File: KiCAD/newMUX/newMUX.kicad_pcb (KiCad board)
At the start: 4 copper layers, 40 x 89 mm, 36 parts, among them J1 Conn_01x14, J2 Conn_02x06_Odd_Even, J3 Conn_02x06_Odd_Even, J4 Conn_01x14, U1 ASSR-1611, U10 ASSR-1611, U11 ASSR-1611, U12 ASSR-1611, U13 ASSR-1611, U14 ASSR-1611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

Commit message: wip for base1x
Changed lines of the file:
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@@
   (general
     (thickness 1.6)
-    (drawings 9)
+    (drawings 17)
     (tracks 698)
     (zones 0)
@@
     (tags "resistor 2010")
     (attr smd)
-    (fp_text reference R1 (at 0 2.54 90) (layer F.SilkS)
+    (fp_text reference R1 (at 0.81 -2.7 90) (layer F.SilkS)
       (effects (font (size 1 1) (thickness 0.15)))
     )
@@
       (xy 8.293997 0.976563) (xy 8.491005 0.779554)) (layer F.SilkS) (width 0.001))
   )
+  (gr_line (start 14 14) (end 14 -14) (layer F.SilkS) (width 0.2))
+  (gr_line (start -14 14) (end 14 14) (layer F.SilkS) (width 0.2))
+  (gr_line (start -14 -14) (end -14 14) (layer F.SilkS) (width 0.2))
+  (gr_line (start 14 -14) (end -14 -14) (layer F.SilkS) (width 0.2))
+  (gr_line (start -15 15) (end -15 -15) (layer F.SilkS) (width 0.2))
+  (gr_line (start 15 15) (end -15 15) (layer F.SilkS) (width 0.2))
+  (gr_line (start 15 -15) (end 15 15) (layer F.SilkS) (width 0.2))
+  (gr_line (start -15 -15) (end 15 -15) (layer F.SilkS) (width 0.2))
   (gr_arc (start 17.5 42) (end 17.5 44.5) (angle -90) (layer Edge.Cuts) (width 0.15))
   (gr_arc (start -17.5 42) (end -20 42) (angle -90) (layer Edge.Cuts) (width 0.15))

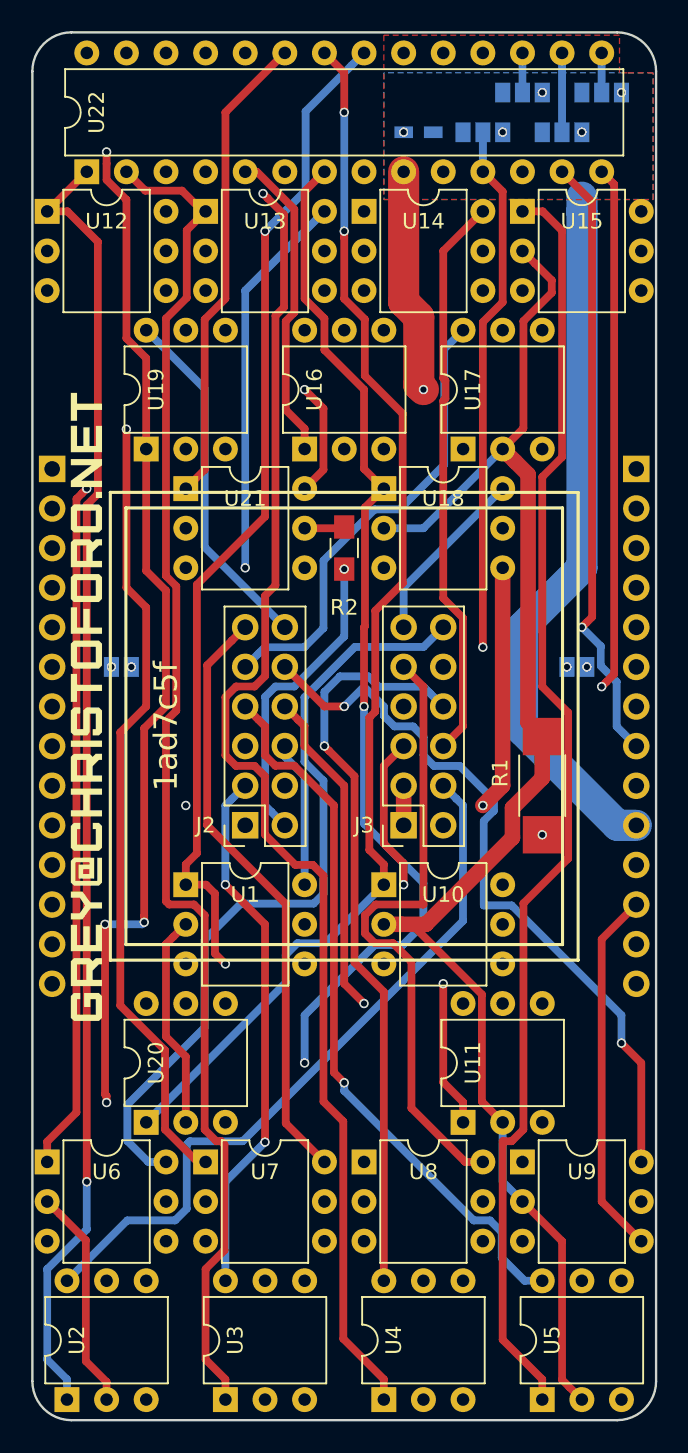
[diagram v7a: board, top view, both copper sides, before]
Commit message: make spring pin board pin holders smaller, update base1x, update mux design controller board
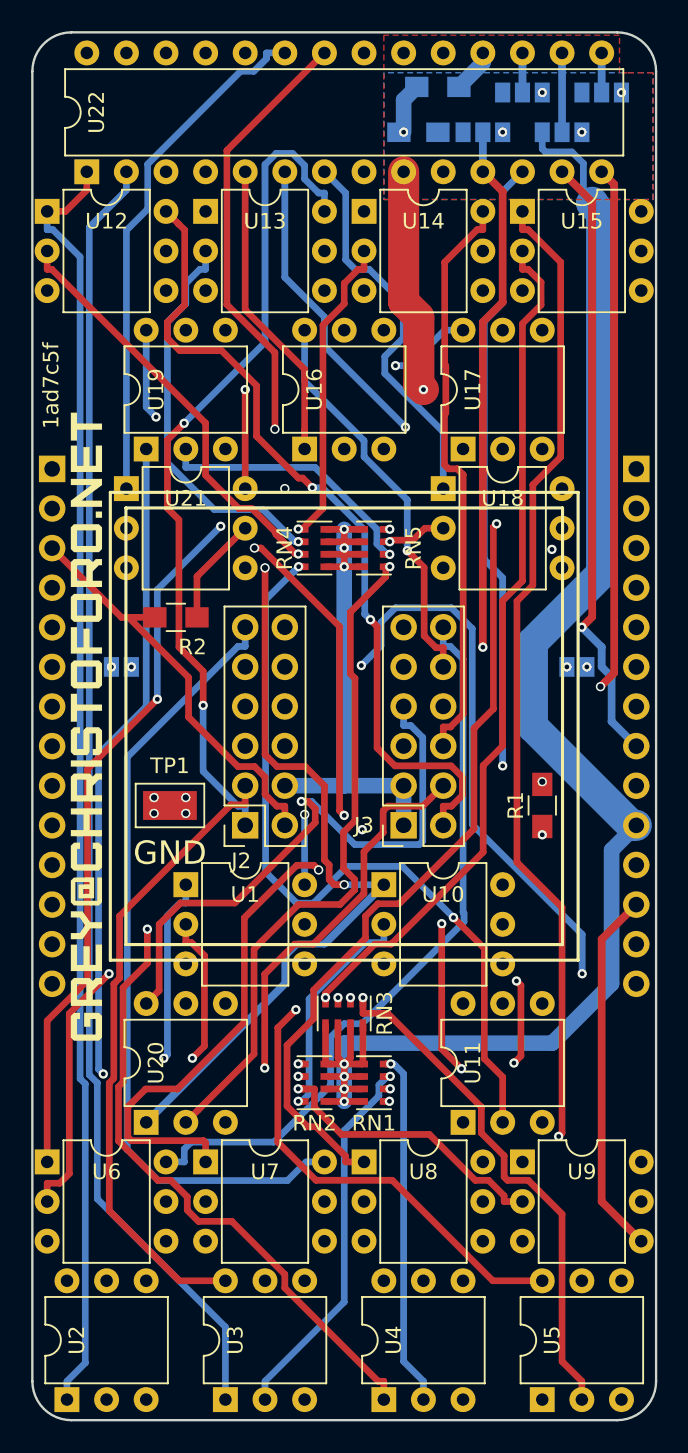
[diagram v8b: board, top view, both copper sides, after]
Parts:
- added R3: 10K, Resistors_SMD:R_0805_HandSoldering, B.Cu at (6.00, -41.0)
- added RN1: 470R, Resistors_SMD:R_Cat16-4, F.Cu at (1.91, 22.9)
- added RN2: 470R, Resistors_SMD:R_Cat16-4, F.Cu at (-1.91, 22.9)
- added RN3: 470R, Resistors_SMD:R_Cat16-4, F.Cu at (0.00, 18.4)
- added RN4: 470R, Resistors_SMD:R_Cat16-4, F.Cu at (-1.91, -11.4)
- added RN5: 470R, Resistors_SMD:R_Cat16-4, F.Cu at (1.91, -11.4)
- added TP1: Test_Point, myParts:Test_Point_S1751-46R, F.Cu at (-11.2, 5.08)
- C1: footprint Capacitors_SMD:C_0603_HandSoldering -> Capacitors_SMD:C_0805_HandSoldering
- R1: value 830K -> 470R; footprint Resistors_SMD:R_2010_HandSoldering -> Resistors_SMD:R_0805_HandSoldering
- moved R2 11.7 mm to (-10.8, -6.99), turned to 180 degrees
- moved U21 3.81 mm to (-14.0, -15.2)
- moved U18 3.81 mm to (6.35, -15.2)
- moved L1 1.27 mm to (-16.5, 0.00)
- moved R1 1.27 mm to (12.7, 5.08)
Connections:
- R1 pad 2: /PRE_GND -> Net-(R1-Pad2)
- U1 pad 2: /PRE_GND -> Net-(RN1-Pad1)
- U1 pad 3: Net-(U1-Pad3) -> (no net)
- U1 pad 5: Net-(U1-Pad5) -> (no net)
- U10 pad 2: /PRE_GND -> Net-(RN2-Pad8)
- U10 pad 3: Net-(U10-Pad3) -> (no net)
- U10 pad 5: Net-(U10-Pad5) -> (no net)
- U11 pad 2: /PRE_GND -> Net-(RN4-Pad4)
- U11 pad 3: Net-(U11-Pad3) -> (no net)
- U11 pad 5: Net-(U11-Pad5) -> (no net)
- U12 pad 2: /PRE_GND -> Net-(RN4-Pad3)
- U12 pad 3: Net-(U12-Pad3) -> (no net)
- U12 pad 5: Net-(U12-Pad5) -> (no net)
- U13 pad 2: /PRE_GND -> Net-(RN4-Pad2)
- U13 pad 3: Net-(U13-Pad3) -> (no net)
- U13 pad 5: Net-(U13-Pad5) -> (no net)
- U14 pad 2: /PRE_GND -> Net-(RN4-Pad1)
- U14 pad 3: Net-(U14-Pad3) -> (no net)
- U14 pad 5: Net-(U14-Pad5) -> (no net)
- U15 pad 2: /PRE_GND -> Net-(RN3-Pad4)
- U15 pad 3: Net-(U15-Pad3) -> (no net)
- U15 pad 5: Net-(U15-Pad5) -> (no net)
- U16 pad 2: /PRE_GND -> Net-(RN3-Pad3)
- U16 pad 3: Net-(U16-Pad3) -> (no net)
- U16 pad 5: Net-(U16-Pad5) -> (no net)
- U17 pad 2: /PRE_GND -> Net-(RN5-Pad8)
- U17 pad 3: Net-(U17-Pad3) -> (no net)
- U17 pad 5: Net-(U17-Pad5) -> (no net)
- U18 pad 2: /PRE_GND -> Net-(RN5-Pad7)
- U18 pad 3: Net-(U18-Pad3) -> (no net)
- U18 pad 5: Net-(U18-Pad5) -> (no net)
- U19 pad 2: /PRE_GND -> Net-(RN5-Pad6)
- U19 pad 3: Net-(U19-Pad3) -> (no net)
- U19 pad 5: Net-(U19-Pad5) -> (no net)
- U2 pad 2: /PRE_GND -> Net-(RN1-Pad2)
- U2 pad 3: Net-(U2-Pad3) -> (no net)
- U2 pad 5: Net-(U2-Pad5) -> (no net)
- U20 pad 2: /PRE_GND -> Net-(RN5-Pad5)
- U20 pad 3: Net-(U20-Pad3) -> (no net)
- U20 pad 5: Net-(U20-Pad5) -> (no net)
- U21 pad 2: /PRE_GND -> Net-(R1-Pad2)
- U21 pad 3: Net-(U21-Pad3) -> (no net)
- U21 pad 4: Net-(U21-Pad4) -> (no net)
- U22 pad 18: +5V -> Net-(R3-Pad2)
- U22 pad 19: Net-(U22-Pad19) -> (no net)
- U22 pad 20: Net-(U22-Pad20) -> (no net)
- U22 pad 24: Net-(U22-Pad24) -> (no net)
- U22 pad 25: Net-(U22-Pad25) -> (no net)
- U22 pad 26: Net-(U22-Pad26) -> (no net)
- U22 pad 27: Net-(U22-Pad27) -> (no net)
- U22 pad 28: Net-(U22-Pad28) -> (no net)
- U3 pad 2: /PRE_GND -> Net-(RN1-Pad3)
- U3 pad 3: Net-(U3-Pad3) -> (no net)
- U3 pad 5: Net-(U3-Pad5) -> (no net)
- U4 pad 2: /PRE_GND -> Net-(RN1-Pad4)
- U4 pad 3: Net-(U4-Pad3) -> (no net)
- U4 pad 5: Net-(U4-Pad5) -> (no net)
- U5 pad 2: /PRE_GND -> Net-(RN3-Pad1)
- U5 pad 3: Net-(U5-Pad3) -> (no net)
- U5 pad 5: Net-(U5-Pad5) -> (no net)
- U6 pad 2: /PRE_GND -> Net-(RN3-Pad2)
- U6 pad 3: Net-(U6-Pad3) -> (no net)
- U6 pad 5: Net-(U6-Pad5) -> (no net)
- U7 pad 2: /PRE_GND -> Net-(RN2-Pad5)
- U7 pad 3: Net-(U7-Pad3) -> (no net)
- U7 pad 5: Net-(U7-Pad5) -> (no net)
- U8 pad 2: /PRE_GND -> Net-(RN2-Pad6)
- U8 pad 3: Net-(U8-Pad3) -> (no net)
- U8 pad 5: Net-(U8-Pad5) -> (no net)
- U9 pad 2: /PRE_GND -> Net-(RN2-Pad7)
- U9 pad 3: Net-(U9-Pad3) -> (no net)
- U9 pad 5: Net-(U9-Pad5) -> (no net)
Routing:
- net /PRE_GND: track 281.3 -> 0.00 mm
- net GND: track 96.9 -> 207.1 mm, vias 1 -> 12
- net Net-(RN3-Pad4): track 0.00 -> 55.2 mm, vias 0 -> 1
- net Net-(RN4-Pad4): track 0.00 -> 50.5 mm, vias 0 -> 2
- net Net-(RN5-Pad5): track 0.00 -> 43.6 mm, vias 0 -> 1
- net Net-(R1-Pad2): track 0.00 -> 42.6 mm, vias 0 -> 3
- net Net-(RN3-Pad3): track 0.00 -> 38.9 mm, vias 0 -> 1
- net Net-(RN3-Pad2): track 0.00 -> 33.8 mm, vias 0 -> 2
- net Net-(RN3-Pad1): track 0.00 -> 33.3 mm, vias 0 -> 1
- net Net-(RN1-Pad2): track 0.00 -> 28.5 mm, vias 0 -> 1
- net Net-(RN4-Pad3): track 0.00 -> 27.2 mm, vias 0 -> 1
- net Net-(RN1-Pad1): track 0.00 -> 26.9 mm, vias 0 -> 2
- net Net-(RN4-Pad2): track 0.00 -> 25.6 mm, vias 0 -> 1
- net Net-(RN1-Pad3): track 0.00 -> 24.4 mm, vias 0 -> 1
- net Net-(RN1-Pad4): track 0.00 -> 22.8 mm, vias 0 -> 1
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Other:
- board text added: "GND"
